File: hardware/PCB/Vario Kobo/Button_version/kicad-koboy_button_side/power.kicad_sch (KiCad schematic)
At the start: 6 parts

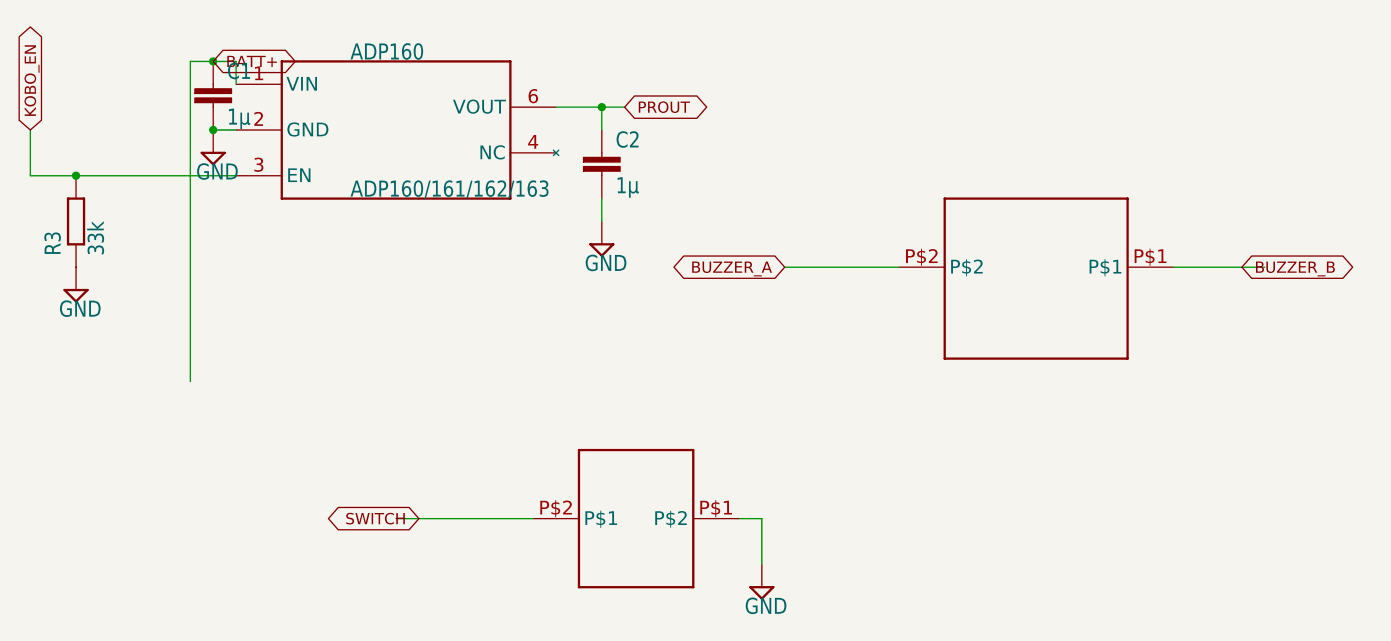
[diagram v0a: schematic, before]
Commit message: Restructure Vario Kobo schematic into main + power supply sheets
- Rename the KiCad project to main (main.kicad_pro/.kicad_sch/.kicad_pcb)
  and drop the empty "Alimentation" top-level sheet left by the Eagle import.
- Move the ADP160 regulator (R3, C1, C2) into a "Power supply" sub-sheet.
- Redraw the main sheet on A3 by function (barometer, Kobo connector + GPS,
  programming/MCLR, button, MAS6240 audio) with net labels instead of long
  wires, and add design notes per block.
- Add no-connect flags and PWR_FLAGs: ERC goes from 20 violations to
  11 warnings (Eagle pin types), no errors.
- Update the PCB from the schematic (renamed nets, same routing).
- README: refresh the ERC/DRC open issues and the project path.

Netlist topology, values and footprints are unchanged.

Co-Authored-By: Claude Opus 5.5 <noreply@anthropic.com>
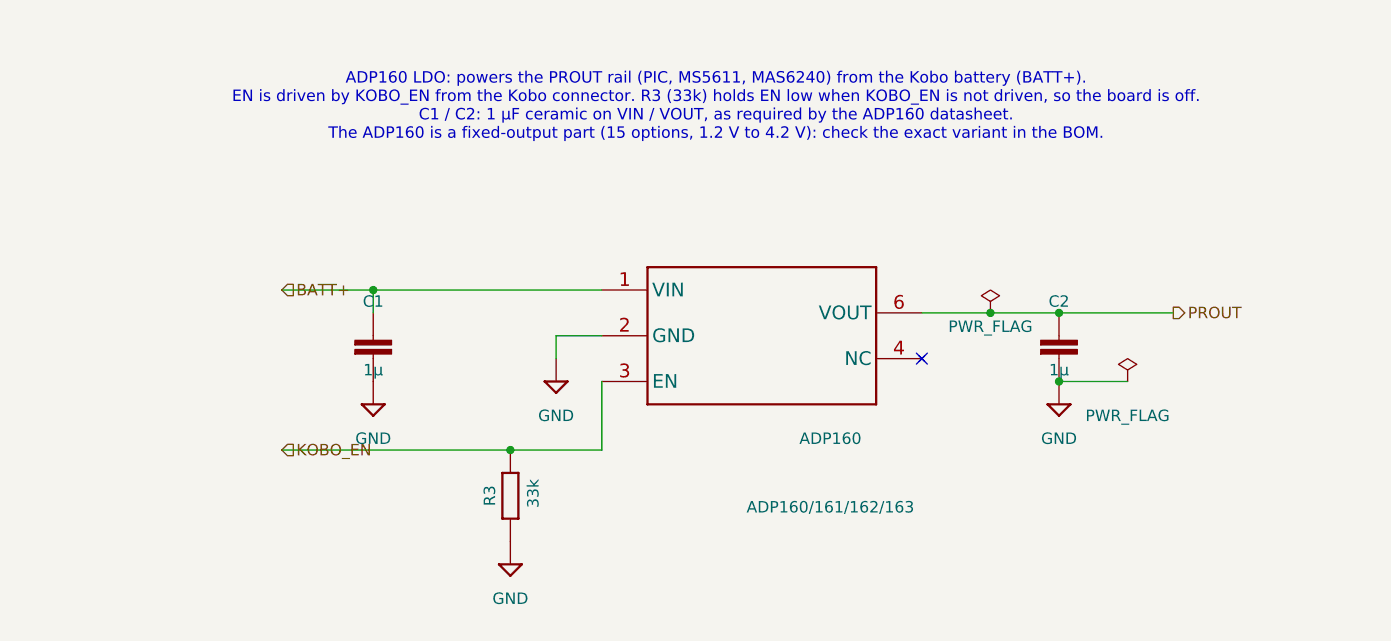
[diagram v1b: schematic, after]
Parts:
- removed BUTTON0: SMS_J_LEAD, Vario Kobo-import-fps:SMS_J_LEAD, symbol Vario Kobo-eagle-import:SMS_J_LEAD
- removed BUZZER0: PKLCS1212E2000-R1, Vario Kobo-import-fps:PKLCS1212E2000-R1-SMD, symbol Vario Kobo-eagle-import:PKLCS1212E2000-R1
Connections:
- no-connect marks 0 -> 1
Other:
- note added: "ADP160 LDO: powers the PROUT rail (PIC, MS5611, MAS6240) from the Kobo battery (BATT+). EN is driven by KOBO_EN from the Kobo connector. R3 (33k) holds EN low when KOBO_EN is not driven, so the board is off. C1 / C2: 1 µF ceramic on VIN / VOUT, as required by the ADP160 datasheet. The ADP160 is a fixed-output part (15 options, 1.2 V to 4.2 V): check the exact variant in the BOM."

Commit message: Rename references and lay out a readable silkscreen
- Rename the Eagle-style references to short standard ones:
  PIC0->U1, MS5611->U2, MAS0->U3, ADP160->U4, PA6H0->U5,
  CONN_KOBO0->J1, CONN_PROG0->J2, BUTTON0->SW1, BUZZER0->BZ1.
- Move every footprint reference field next to its part, 0.8 mm text,
  clear of pads, vias and the board edge, closer to its own part than
  to any other one.
- Add footprint-owned silkscreen texts: J1/J2 pin names and a "1" next
  to pin 1 of U1-U5, so they follow the parts if they move.
- Hide value fields; drop the Eagle "1" next to the GPS and move the U1
  "*" mark to F.Fab.
- README: DRC is down from 74 to 22 warnings (footprint outlines over pads).

Co-Authored-By: Claude Opus 5.5 <noreply@anthropic.com>
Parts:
- renumbered ADP160 to U4
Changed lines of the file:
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@@
 		(in_pos_files yes)
 		(dnp no)
-		(property "Reference" "ADP160"
+		(property "Reference" "U4"
 			(at 165.1 118.11 0)
 			(show_name no)
@@
 			(project "main"
 				(path "/3589bf9b-6637-4745-bf4f-b7acb8d1884d/9b1d1e6a-e9ed-416c-b565-a066b307f2c4"
-					(reference "ADP160")
+					(reference "U4")
 					(unit 1)
 				)
@@
 			(project "Vario Kobo"
 				(path "/cad23409-104e-4581-9266-d814992be1c5/9b1d1e6a-e9ed-416c-b565-a066b307f2c4"
-					(reference "ADP160")
+					(reference "U4")
 					(unit 1)
 				)

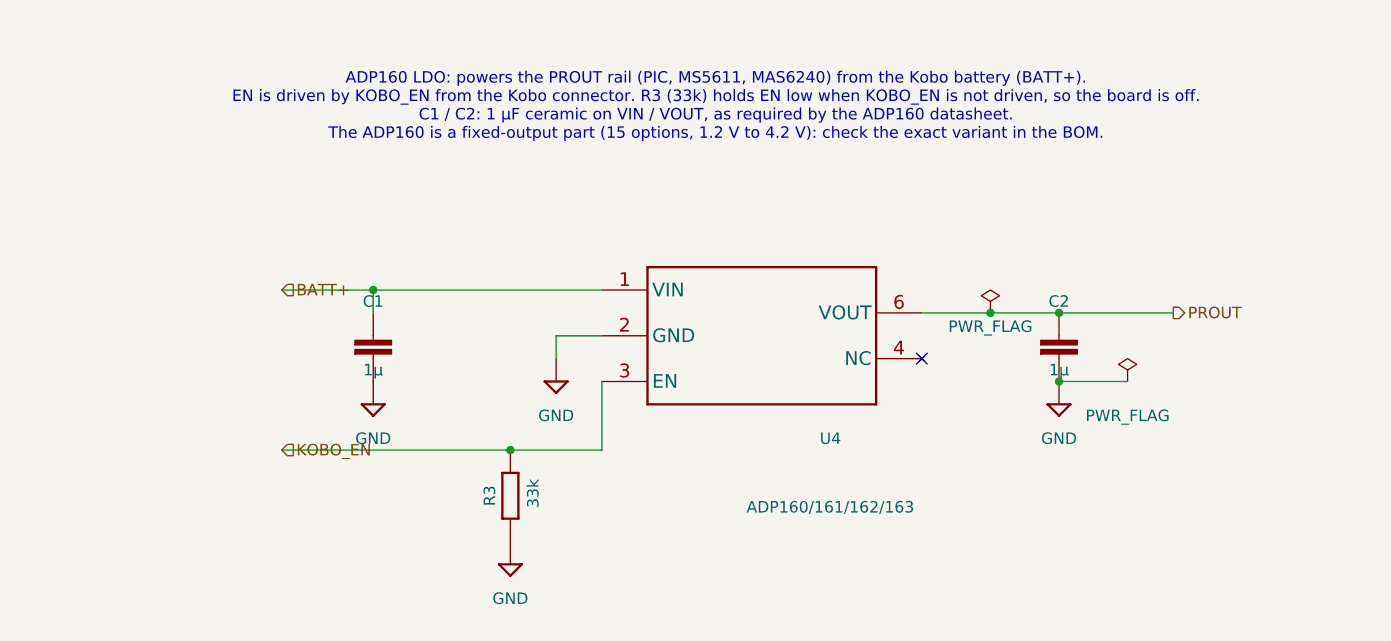
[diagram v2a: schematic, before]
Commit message: Use Gekkio's FGPMMOPA6H for the GPS and clean up ERC
- U5 (GPS): replace the Eagle PA6H symbol and footprint with Gekkio's
  FGPMMOPA6H (gekkio-kicad-libs, CC BY 4.0, copied into libs/gekkio/ and
  registered in the project library tables). Same pad geometry; adds the
  datasheet's 1.2 mm NPTH under the module, a courtyard and a silkscreen
  outline clear of the pads. Unused pins flagged no-connect (datasheet:
  leave floating).
- Fix pin electrical types in the Eagle-imported symbols (connectors and
  switch passive, MAS6240/ADP160 power pins power in/out), add PWR_FLAGs
  on BATT+ and KOBO_EN, drop the now redundant one on PROUT.
- ERC: 0 errors, 0 warnings. DRC: 2 warnings (buzzer outline), no errors.
- README: refresh open issues, credit Gekkio. Ignore *.bak.

Co-Authored-By: Claude Opus 5.5 <noreply@anthropic.com>
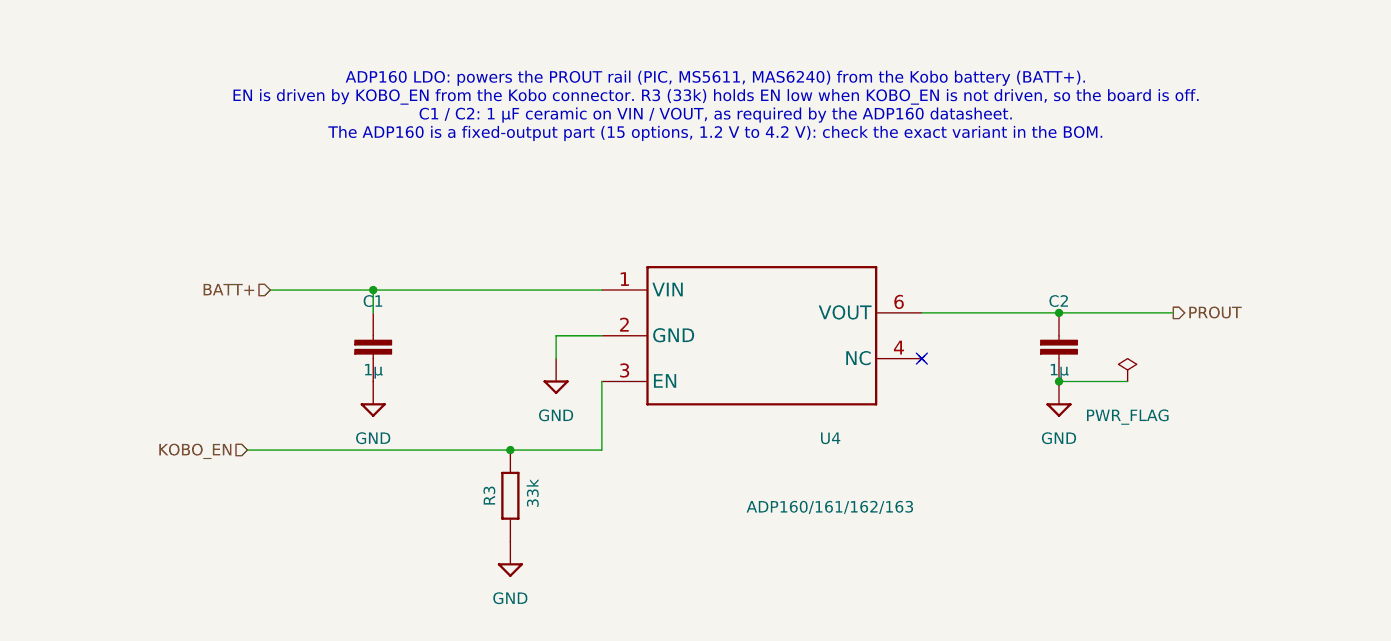
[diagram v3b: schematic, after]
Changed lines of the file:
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@@
-	)
-	(junction
-		(at 182.88 104.14)
-		(diameter 0)
-		(color 0 0 0 0)
 	)
 	(junction
@@
 	(wire
 		(pts
-			(xy 129.54 119.38) (xy 104.14 119.38)
+			(xy 100.33 119.38) (xy 129.54 119.38)
 		)
 		(stroke
@@
 	(wire
 		(pts
-			(xy 175.26 104.14) (xy 182.88 104.14)
-		)
-		(stroke
-			(width 0)
-			(type default)
-		)
-	)
-	(wire
-		(pts
-			(xy 182.88 104.14) (xy 190.5 104.14)
-		)
-		(stroke
-			(width 0)
-			(type default)
-		)
-	)
-	(wire
-		(pts
-			(xy 104.14 101.6) (xy 114.3 101.6)
+			(xy 175.26 104.14) (xy 190.5 104.14)
+		)
+		(stroke
+			(width 0)
+			(type default)
+		)
+	)
+	(wire
+		(pts
+			(xy 102.87 101.6) (xy 114.3 101.6)
 		)
 		(stroke
@@
 				(size 1.27 1.27)
 			)
+			(justify left)
 		)
 	)
 	(hierarchical_label "KOBO_EN"
 		(shape input)
-		(at 104.14 119.38 0)
+		(at 100.33 119.38 180)
 		(effects
 			(font
 				(size 1.27 1.27)
 			)
+			(justify right)
 		)
 	)
 	(hierarchical_label "BATT+"
 		(shape input)
-		(at 104.14 101.6 0)
+		(at 102.87 101.6 180)
 		(effects
 			(font
 				(size 1.27 1.27)
 			)
+			(justify right)
 		)
 	)
 	(symbol
-		(lib_name "R-EU_R0603")
 		(lib_id "Vario Kobo-eagle-import:R-EU_R0603")
 		(at 129.54 124.46 90)
@@
 		(instances
 			(project "main"
-				(path "/3589bf9b-6637-4745-bf4f-b7acb8d1884d/9b1d1e6a-e9ed-416c-b565-a066b307f2c4"
-					(reference "R3")
-					(unit 1)
-				)
-			)
-			(project "Vario Kobo"
 				(path "/cad23409-104e-4581-9266-d814992be1c5/9b1d1e6a-e9ed-416c-b565-a066b307f2c4"
 					(reference "R3")
@@
 	)
 	(symbol
-		(lib_name "GND")
 		(lib_id "Vario Kobo-eagle-import:GND")
 		(at 134.62 111.76 0)
@@
 		(instances
 			(project "main"
-				(path "/3589bf9b-6637-4745-bf4f-b7acb8d1884d/9b1d1e6a-e9ed-416c-b565-a066b307f2c4"
-					(reference "#SUPPLY19")
-					(unit 1)
-				)
-			)
-			(project "Vario Kobo"
 				(path "/cad23409-104e-4581-9266-d814992be1c5/9b1d1e6a-e9ed-416c-b565-a066b307f2c4"
 					(reference "#SUPPLY19")
@@
 	)
 	(symbol
-		(lib_id "power:PWR_FLAG")
-		(at 182.88 104.14 0)
-		(unit 1)
-		(body_style 1)
-		(exclude_from_sim no)
-		(in_bom yes)
-		(on_board yes)
-		(in_pos_files yes)
-		(dnp no)
-		(property "Reference" "#FLG01"
-			(at 182.88 100.33 0)
-			(hide yes)
-			(show_name no)
-			(do_not_autoplace no)
-			(effects
-				(font
-					(size 1.27 1.27)
-				)
-			)
-		)
-		(property "Value" "PWR_FLAG"
-			(at 182.88 105.664 0)
-			(show_name no)
-			(do_not_autoplace no)
-			(effects
-				(font
-					(size 1.27 1.27)
-				)
-			)
-		)
-		(property "Footprint" ""
-			(at 182.88 104.14 0)
-			(hide yes)
-			(show_name no)
-			(do_not_autoplace no)
-			(effects
-				(font
-					(size 1.27 1.27)
-				)
-			)
-		)
-		(property "Datasheet" ""
-			(at 182.88 104.14 0)
-			(hide yes)
-			(show_name no)
-			(do_not_autoplace no)
-			(effects
-				(font
-					(size 1.27 1.27)
-				)
-			)
-		)
-		(property "Description" ""
-			(at 182.88 104.14 0)
-			(show_name no)
-			(do_not_autoplace no)
-			(effects
-				(font
-					(size 1.27 1.27)
-				)
-			)
-		)
-		(pin "1"
-		)
-		(instances
-			(project "main"
-				(path "/3589bf9b-6637-4745-bf4f-b7acb8d1884d/9b1d1e6a-e9ed-416c-b565-a066b307f2c4"
-					(reference "#FLG01")
-					(unit 1)
-				)
-			)
-			(project "Vario Kobo"
-				(path "/cad23409-104e-4581-9266-d814992be1c5/9b1d1e6a-e9ed-416c-b565-a066b307f2c4"
-					(reference "#FLG01")
-					(unit 1)
-				)
-			)
-		)
-	)
-	(symbol
-		(lib_name "ADP160/161/162/163")
 		(lib_id "Vario Kobo-eagle-import:ADP160/161/162/163")
 		(at 165.1 121.92 0)
@@
 		(instances
 			(project "main"
-				(path "/3589bf9b-6637-4745-bf4f-b7acb8d1884d/9b1d1e6a-e9ed-416c-b565-a066b307f2c4"
-					(reference "U4")
-					(unit 1)
-				)
-			)
-			(project "Vario Kobo"
 				(path "/cad23409-104e-4581-9266-d814992be1c5/9b1d1e6a-e9ed-416c-b565-a066b307f2c4"
 					(reference "U4")
@@
 		(property "Description" ""
 			(at 198.12 111.76 0)
+			(hide yes)
 			(show_name no)
 			(do_not_autoplace no)
@@
 		(instances
 			(project "main"
-				(path "/3589bf9b-6637-4745-bf4f-b7acb8d1884d/9b1d1e6a-e9ed-416c-b565-a066b307f2c4"
-					(reference "#FLG02")
-					(unit 1)
-				)
-			)
-			(project "Vario Kobo"
 				(path "/cad23409-104e-4581-9266-d814992be1c5/9b1d1e6a-e9ed-416c-b565-a066b307f2c4"
 					(reference "#FLG02")
@@
 	)
 	(symbol
-		(lib_name "C-EUC0603")
 		(lib_id "Vario Kobo-eagle-import:C-EUC0603")
 		(at 190.5 106.68 0)
@@
 		(instances
 			(project "main"
-				(path "/3589bf9b-6637-4745-bf4f-b7acb8d1884d/9b1d1e6a-e9ed-416c-b565-a066b307f2c4"
-					(reference "C2")
-					(unit 1)
-				)
-			)
-			(project "Vario Kobo"
 				(path "/cad23409-104e-4581-9266-d814992be1c5/9b1d1e6a-e9ed-416c-b565-a066b307f2c4"
 					(reference "C2")
@@
 	)
 	(symbol
-		(lib_name "GND")
 		(lib_id "Vario Kobo-eagle-import:GND")
 		(at 129.54 132.08 0)
@@
 		(instances
 			(project "main"
-				(path "/3589bf9b-6637-4745-bf4f-b7acb8d1884d/9b1d1e6a-e9ed-416c-b565-a066b307f2c4"
-					(reference "#SUPPLY1")
-					(unit 1)
-				)
-			)
-			(project "Vario Kobo"
 				(path "/cad23409-104e-4581-9266-d814992be1c5/9b1d1e6a-e9ed-416c-b565-a066b307f2c4"
 					(reference "#SUPPLY1")
@@
 	)
 	(symbol
-		(lib_name "GND")
 		(lib_id "Vario Kobo-eagle-import:GND")
 		(at 114.3 114.3 0)
@@
 		(instances
 			(project "main"
-				(path "/3589bf9b-6637-4745-bf4f-b7acb8d1884d/9b1d1e6a-e9ed-416c-b565-a066b307f2c4"
-					(reference "#SUPPLY14")
-					(unit 1)
-				)
-			)
-			(project "Vario Kobo"
 				(path "/cad23409-104e-4581-9266-d814992be1c5/9b1d1e6a-e9ed-416c-b565-a066b307f2c4"
 					(reference "#SUPPLY14")
@@
 	)
 	(symbol
-		(lib_name "GND")
 		(lib_id "Vario Kobo-eagle-import:GND")
 		(at 190.5 114.3 0)
@@
 		(instances
 			(project "main"
-				(path "/3589bf9b-6637-4745-bf4f-b7acb8d1884d/9b1d1e6a-e9ed-416c-b565-a066b307f2c4"
-					(reference "#SUPPLY15")
-					(unit 1)
-				)
-			)
-			(project "Vario Kobo"
 				(path "/cad23409-104e-4581-9266-d814992be1c5/9b1d1e6a-e9ed-416c-b565-a066b307f2c4"
 					(reference "#SUPPLY15")
@@
 	)
 	(symbol
-		(lib_name "C-EUC0603")
 		(lib_id "Vario Kobo-eagle-import:C-EUC0603")
 		(at 114.3 106.68 0)
@@
 		(instances
 			(project "main"
-				(path "/3589bf9b-6637-4745-bf4f-b7acb8d1884d/9b1d1e6a-e9ed-416c-b565-a066b307f2c4"
-					(reference "C1")
-					(unit 1)
-				)
-			)
-			(project "Vario Kobo"
 				(path "/cad23409-104e-4581-9266-d814992be1c5/9b1d1e6a-e9ed-416c-b565-a066b307f2c4"
 					(reference "C1")

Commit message: Use KiCad's standard 0603 HandSolder footprints for R and C
Replace the Eagle-imported R0603/C0603 footprints of R1-R7 and C1-C8
with Resistor_SMD:R_0603_1608Metric_Pad0.98x0.95mm_HandSolder and
Capacitor_SMD:C_0603_1608Metric_Pad1.08x0.95mm_HandSolder, easier to
solder by hand. Footprint positions and routing are unchanged; the
track ends still land inside the new pads.

Reference fields are put back at their 0.8 mm silkscreen spots and all
Value fields are hidden on F.Fab (U2's moved off F.Silkscreen too).
Netlist topology unchanged, ERC 0, DRC 0 errors / 2 warnings (BZ1 outline).

Co-Authored-By: Claude Opus 5.5 <noreply@anthropic.com>
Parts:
- C1, C2: footprint Vario Kobo-import-fps:C0603 -> Capacitor_SMD:C_0603_1608Metric_Pad1.08x0.95mm_HandSolder
- R3: footprint Vario Kobo-import-fps:R0603 -> Resistor_SMD:R_0603_1608Metric_Pad0.98x0.95mm_HandSolder
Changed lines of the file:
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@@
 			)
 		)
-		(property "Footprint" "Vario Kobo-import-fps:R0603"
+		(property "Footprint" "Resistor_SMD:R_0603_1608Metric_Pad0.98x0.95mm_HandSolder"
 			(at 129.54 124.46 0)
 			(hide yes)
@@
 			)
 		)
-		(property "Footprint" "Vario Kobo-import-fps:C0603"
+		(property "Footprint" "Capacitor_SMD:C_0603_1608Metric_Pad1.08x0.95mm_HandSolder"
 			(at 190.5 106.68 0)
 			(hide yes)
@@
 			)
 		)
-		(property "Footprint" "Vario Kobo-import-fps:C0603"
+		(property "Footprint" "Capacitor_SMD:C_0603_1608Metric_Pad1.08x0.95mm_HandSolder"
 			(at 114.3 106.68 0)
 			(hide yes)
